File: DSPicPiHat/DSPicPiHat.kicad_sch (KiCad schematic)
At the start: 77 parts, among them J1 Conn_01x09_Female, J4 Conn_PIC_ICSP_ICD, J5 USB_C_Receptacle_USB2.0, J6 PowerInput, J8 RasPiHeaders, SW1 POWER_Select, SW2 SW_DIP_x08, U1 DSPIC33CH512MP508T-I_PT, U10 DF5A6.2CJE_LM, U11 FT230XS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

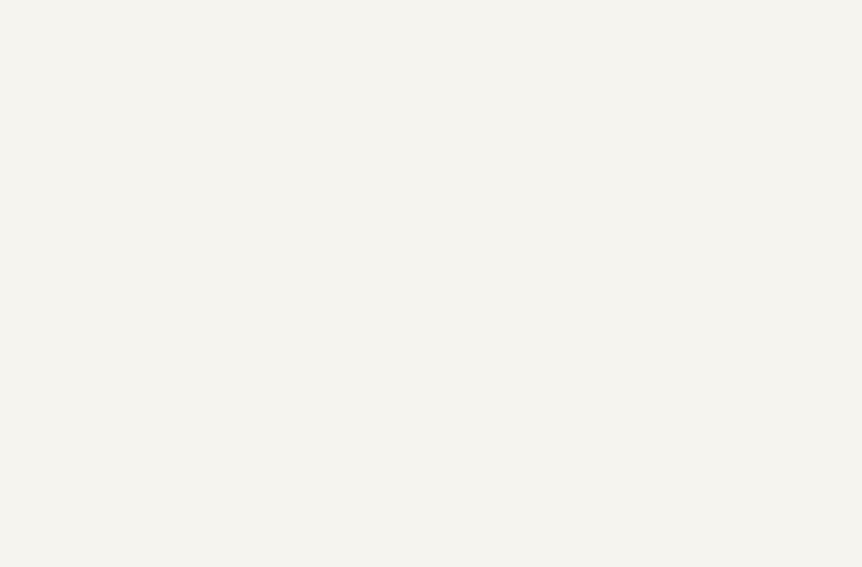
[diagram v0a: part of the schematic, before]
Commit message: Grounded mounting points
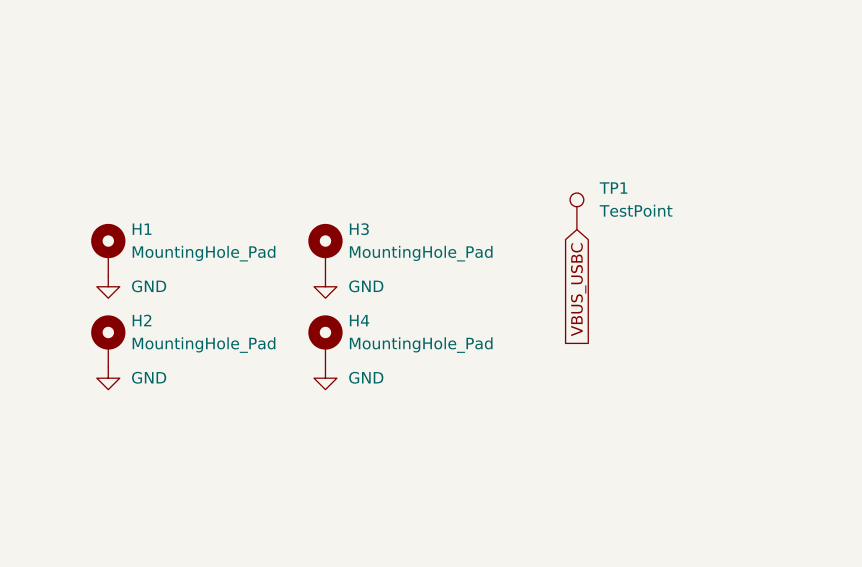
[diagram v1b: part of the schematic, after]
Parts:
- added H1, H2, H3, H4: MountingHole_Pad, MountingHole:MountingHole_2.7mm_M2.5_DIN965_Pad, symbol Mechanical:MountingHole_Pad
- added TP1: TestPoint, TestPoint:TestPoint_Pad_D1.0mm, symbol Connector:TestPoint
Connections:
- net GND: now also H1.1, H2.1, H3.1, H4.1
- net VBUS_USBC: now also TP1.1
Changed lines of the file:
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@@
     )
   )
+  (global_label "VBUS_USBC" (shape input) (at 73.66 175.26 270) (fields_autoplaced)
+    (effects (font (size 1.27 1.27)) (justify right))
+    (property "Intersheet References" "${INTERSHEET_REFS}" (id 0) (at 73.7394 188.6193 90)
+      (effects (font (size 1.27 1.27)) (justify right) hide)
+    )
+  )
   (global_label "GNDZ" (shape input) (at 172.72 261.62 0) (fields_autoplaced)
     (effects (font (size 1.27 1.27)) (justify left))
@@
     (pin "1")
   )
+  (symbol (lib_id "Mechanical:MountingHole_Pad") (at 45.72 177.8 0) (unit 1)
+    (in_bom yes) (on_board yes) (fields_autoplaced)
+    (property "Reference" "H3" (id 0) (at 48.26 175.2599 0)
+      (effects (font (size 1.27 1.27)) (justify left))
+    )
+    (property "Value" "MountingHole_Pad" (id 1) (at 48.26 177.7999 0)
+      (effects (font (size 1.27 1.27)) (justify left))
+    )
+    (property "Footprint" "MountingHole:MountingHole_2.7mm_M2.5_DIN965_Pad" (id 2) (at 45.72 177.8 0)
+      (effects (font (size 1.27 1.27)) hide)
+    )
+    (property "Datasheet" "~" (id 3) (at 45.72 177.8 0)
+      (effects (font (size 1.27 1.27)) hide)
+    )
+    (pin "1")
+  )
   (symbol (lib_id "power:+3V3") (at 163.83 54.61 90) (unit 1)
     (in_bom yes) (on_board yes)
@@
     (pin "1")
   )
+  (symbol (lib_id "power:GND") (at 45.72 180.34 0) (unit 1)
+    (in_bom yes) (on_board yes) (fields_autoplaced)
+    (property "Reference" "#PWR0108" (id 0) (at 45.72 186.69 0)
+      (effects (font (size 1.27 1.27)) hide)
+    )
+    (property "Value" "GND" (id 1) (at 48.26 181.6099 0)
+      (effects (font (size 1.27 1.27)) (justify left))
+    )
+    (property "Footprint" "" (id 2) (at 45.72 180.34 0)
+      (effects (font (size 1.27 1.27)) hide)
+    )
+    (property "Datasheet" "" (id 3) (at 45.72 180.34 0)
+      (effects (font (size 1.27 1.27)) hide)
+    )
+    (pin "1")
+  )
   (symbol (lib_id "Device:LED") (at 273.05 213.36 180) (unit 1)
     (in_bom yes) (on_board yes)
@@
     (pin "2")
   )
+  (symbol (lib_id "Mechanical:MountingHole_Pad") (at 21.59 187.96 0) (unit 1)
+    (in_bom yes) (on_board yes) (fields_autoplaced)
+    (property "Reference" "H2" (id 0) (at 24.13 185.4199 0)
+      (effects (font (size 1.27 1.27)) (justify left))
+    )
+    (property "Value" "MountingHole_Pad" (id 1) (at 24.13 187.9599 0)
+      (effects (font (size 1.27 1.27)) (justify left))
+    )
+    (property "Footprint" "MountingHole:MountingHole_2.7mm_M2.5_DIN965_Pad" (id 2) (at 21.59 187.96 0)
+      (effects (font (size 1.27 1.27)) hide)
+    )
+    (property "Datasheet" "~" (id 3) (at 21.59 187.96 0)
+      (effects (font (size 1.27 1.27)) hide)
+    )
+    (pin "1")
+  )
   (symbol (lib_id "Device:C_Small") (at 139.7 99.06 0) (unit 1)
     (in_bom yes) (on_board yes) (fields_autoplaced)
@@
     (pin "2")
   )
+  (symbol (lib_id "power:GND") (at 45.72 190.5 0) (unit 1)
+    (in_bom yes) (on_board yes) (fields_autoplaced)
+    (property "Reference" "#PWR0107" (id 0) (at 45.72 196.85 0)
+      (effects (font (size 1.27 1.27)) hide)
+    )
+    (property "Value" "GND" (id 1) (at 48.26 191.7699 0)
+      (effects (font (size 1.27 1.27)) (justify left))
+    )
+    (property "Footprint" "" (id 2) (at 45.72 190.5 0)
+      (effects (font (size 1.27 1.27)) hide)
+    )
+    (property "Datasheet" "" (id 3) (at 45.72 190.5 0)
+      (effects (font (size 1.27 1.27)) hide)
+    )
+    (pin "1")
+  )
   (symbol (lib_id "Device:C_Small") (at 375.92 240.03 0) (unit 1)
     (in_bom yes) (on_board yes) (fields_autoplaced)
@@
     (pin "3")
   )
+  (symbol (lib_id "power:GND") (at 21.59 180.34 0) (unit 1)
+    (in_bom yes) (on_board yes) (fields_autoplaced)
+    (property "Reference" "#PWR0106" (id 0) (at 21.59 186.69 0)
+      (effects (font (size 1.27 1.27)) hide)
+    )
+    (property "Value" "GND" (id 1) (at 24.13 181.6099 0)
+      (effects (font (size 1.27 1.27)) (justify left))
+    )
+    (property "Footprint" "" (id 2) (at 21.59 180.34 0)
+      (effects (font (size 1.27 1.27)) hide)
+    )
+    (property "Datasheet" "" (id 3) (at 21.59 180.34 0)
+      (effects (font (size 1.27 1.27)) hide)
+    )
+    (pin "1")
+  )
   (symbol (lib_id "Device:C_Small") (at 167.64 107.95 0) (unit 1)
     (in_bom yes) (on_board yes) (fields_autoplaced)
@@
     (pin "1")
   )
+  (symbol (lib_id "Mechanical:MountingHole_Pad") (at 21.59 177.8 0) (unit 1)
+    (in_bom yes) (on_board yes) (fields_autoplaced)
+    (property "Reference" "H1" (id 0) (at 24.13 175.2599 0)
+      (effects (font (size 1.27 1.27)) (justify left))
+    )
+    (property "Value" "MountingHole_Pad" (id 1) (at 24.13 177.7999 0)
+      (effects (font (size 1.27 1.27)) (justify left))
+    )
+    (property "Footprint" "MountingHole:MountingHole_2.7mm_M2.5_DIN965_Pad" (id 2) (at 21.59 177.8 0)
+      (effects (font (size 1.27 1.27)) hide)
+    )
+    (property "Datasheet" "~" (id 3) (at 21.59 177.8 0)
+      (effects (font (size 1.27 1.27)) hide)
+    )
+    (pin "1")
+  )
   (symbol (lib_id "power:GND") (at 154.94 280.67 0) (unit 1)
     (in_bom yes) (on_board yes)
@@
     (pin "2")
   )
+  (symbol (lib_id "power:GND") (at 21.59 190.5 0) (unit 1)
+    (in_bom yes) (on_board yes) (fields_autoplaced)
+    (property "Reference" "#PWR0105" (id 0) (at 21.59 196.85 0)
+      (effects (font (size 1.27 1.27)) hide)
+    )
+    (property "Value" "GND" (id 1) (at 24.13 191.7699 0)
+      (effects (font (size 1.27 1.27)) (justify left))
+    )
+    (property "Footprint" "" (id 2) (at 21.59 190.5 0)
+      (effects (font (size 1.27 1.27)) hide)
+    )
+    (property "Datasheet" "" (id 3) (at 21.59 190.5 0)
+      (effects (font (size 1.27 1.27)) hide)
+    )
+    (pin "1")
+  )
+  (symbol (lib_id "Mechanical:MountingHole_Pad") (at 45.72 187.96 0) (unit 1)
+    (in_bom yes) (on_board yes) (fields_autoplaced)
+    (property "Reference" "H4" (id 0) (at 48.26 185.4199 0)
+      (effects (font (size 1.27 1.27)) (justify left))
+    )
+    (property "Value" "MountingHole_Pad" (id 1) (at 48.26 187.9599 0)
+      (effects (font (size 1.27 1.27)) (justify left))
+    )
+    (property "Footprint" "MountingHole:MountingHole_2.7mm_M2.5_DIN965_Pad" (id 2) (at 45.72 187.96 0)
+      (effects (font (size 1.27 1.27)) hide)
+    )
+    (property "Datasheet" "~" (id 3) (at 45.72 187.96 0)
+      (effects (font (size 1.27 1.27)) hide)
+    )
+    (pin "1")
+  )
   (symbol (lib_id "power:GND") (at 172.72 25.4 90) (unit 1)
     (in_bom yes) (on_board yes) (fields_autoplaced)
@@
     (pin "1")
   )
+  (symbol (lib_id "Connector:TestPoint") (at 73.66 175.26 0) (unit 1)
+    (in_bom yes) (on_board yes) (fields_autoplaced)
+    (property "Reference" "TP1" (id 0) (at 76.2 170.6879 0)
+      (effects (font (size 1.27 1.27)) (justify left))
+    )
+    (property "Value" "TestPoint" (id 1) (at 76.2 173.2279 0)
+      (effects (font (size 1.27 1.27)) (justify left))
+    )
+    (property "Footprint" "TestPoint:TestPoint_Pad_D1.0mm" (id 2) (at 78.74 175.26 0)
+      (effects (font (size 1.27 1.27)) hide)
+    )
+    (property "Datasheet" "~" (id 3) (at 78.74 175.26 0)
+      (effects (font (size 1.27 1.27)) hide)
+    )
+    (pin "1")
+  )
   (symbol (lib_id "Device:L") (at 148.59 110.49 90) (unit 1)
     (in_bom yes) (on_board yes) (fields_autoplaced)
@@
       (reference "#PWR0104") (unit 1) (value "GND") (footprint "")
     )
+    (path "/a9b95ad6-d018-48b9-a558-775711f89127"
+      (reference "#PWR0105") (unit 1) (value "GND") (footprint "")
+    )
+    (path "/82f23c8b-b869-4a9c-b937-ef0507d0996c"
+      (reference "#PWR0106") (unit 1) (value "GND") (footprint "")
+    )
+    (path "/7ddcd4c2-e959-48b7-9ed7-0c14f86988bc"
+      (reference "#PWR0107") (unit 1) (value "GND") (footprint "")
+    )
+    (path "/2216dda0-4723-4b26-b51f-f57c0d5f596c"
+      (reference "#PWR0108") (unit 1) (value "GND") (footprint "")
+    )
     (path "/bcc72ff3-f25f-4fbf-8751-185f0084a0a5"
       (reference "#PWR0111") (unit 1) (value "GND") (footprint "")
@@
       (reference "FB1") (unit 1) (value "FerriteBead_Small") (footprint "Resistor_SMD:R_1206_3216Metric")
     )
+    (path "/8fd8141b-51d3-4039-9ae2-d935bfece616"
+      (reference "H1") (unit 1) (value "MountingHole_Pad") (footprint "MountingHole:MountingHole_2.7mm_M2.5_DIN965_Pad")
+    )
+    (path "/71258e68-d82e-4695-84af-cece79314b2c"
+      (reference "H2") (unit 1) (value "MountingHole_Pad") (footprint "MountingHole:MountingHole_2.7mm_M2.5_DIN965_Pad")
+    )
+    (path "/1d978e6a-ec49-45d7-a0e4-d16ce34c9343"
+      (reference "H3") (unit 1) (value "MountingHole_Pad") (footprint "MountingHole:MountingHole_2.7mm_M2.5_DIN965_Pad")
+    )
+    (path "/a9ba8de6-1c29-490d-87cf-1f04a7cd1d6b"
+      (reference "H4") (unit 1) (value "MountingHole_Pad") (footprint "MountingHole:MountingHole_2.7mm_M2.5_DIN965_Pad")
+    )
     (path "/c3608861-215c-488a-a792-d96a54902bf7"
       (reference "J1") (unit 1) (value "Conn_01x09_Female") (footprint "Connector_PinHeader_2.54mm:PinHeader_1x09_P2.54mm_Vertical")
@@
       (reference "SW2") (unit 1) (value "SW_DIP_x08") (footprint "Button_Switch_THT:SW_DIP_SPSTx08_Slide_9.78x22.5mm_W7.62mm_P2.54mm")
     )
+    (path "/c9f04593-2c4a-490d-9b24-3e74cd6c1df4"
+      (reference "TP1") (unit 1) (value "TestPoint") (footprint "TestPoint:TestPoint_Pad_D1.0mm")
+    )
     (path "/b5e9c2a5-638a-45da-ac8c-23aea09c1940"

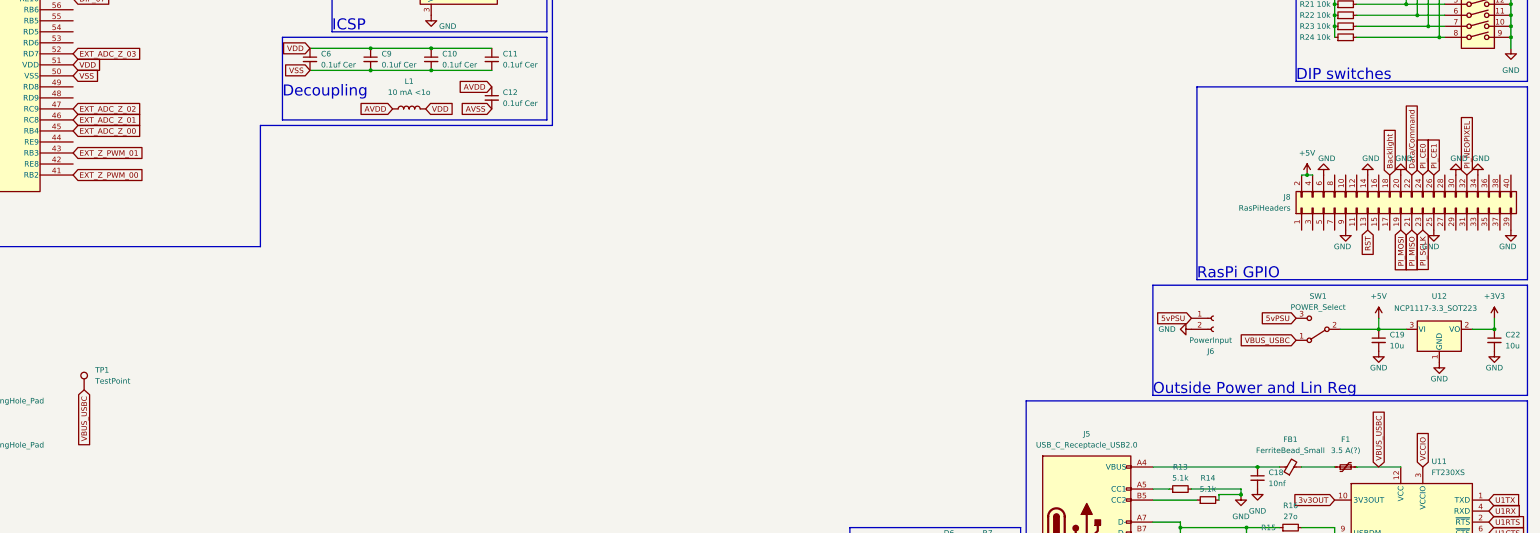
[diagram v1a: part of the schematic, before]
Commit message: Fixed pi header connections
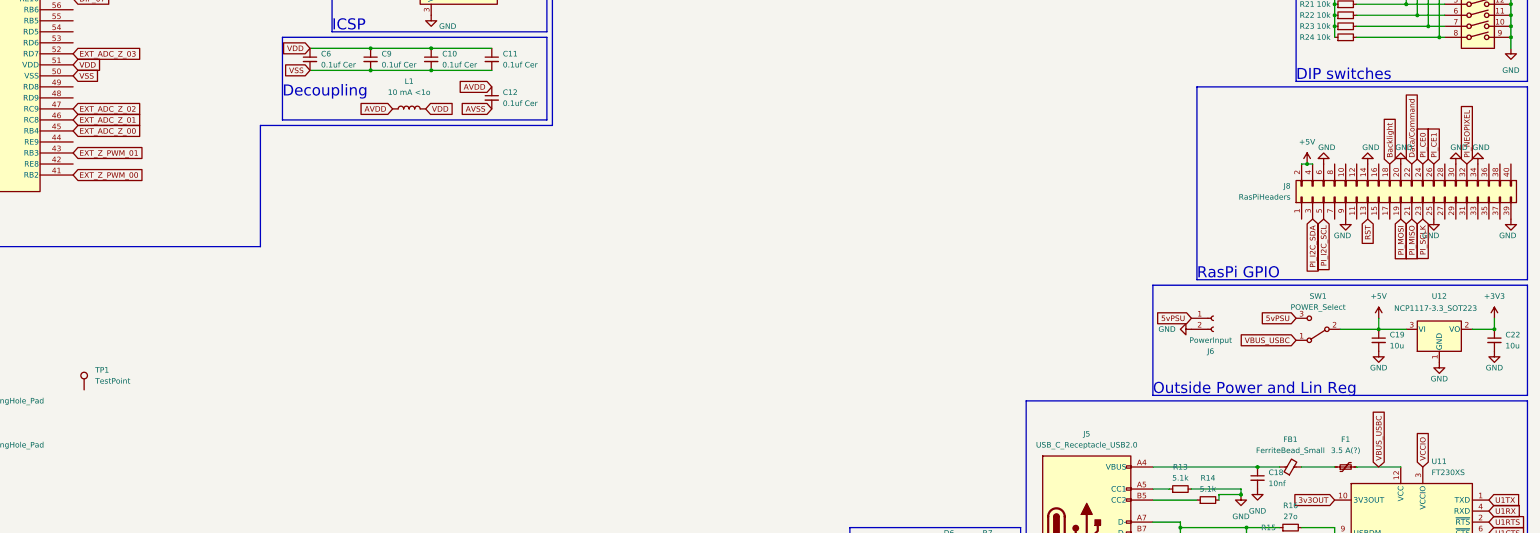
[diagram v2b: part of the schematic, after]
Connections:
- net VBUS_USBC: no longer TP1.1
- net PI_I2C_SDA: now reaches J8.3 (Pin_3)
- net PI_I2C_SCL: now reaches J8.5 (Pin_5)
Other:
- moved on the sheet: J8
